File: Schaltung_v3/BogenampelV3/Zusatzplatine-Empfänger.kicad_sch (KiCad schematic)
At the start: 17 parts, among them J1 5V USB, J2 Poti 47k, J3 Poti 47k, J4 12V DCDC Boost, J5 BTN, J6 Piezo Transducter 12V, J7 LED Stripe, J8 12V FAN, Q1 BC337, U1 TSR0.5-2433, U2 XIAO ESP32C3

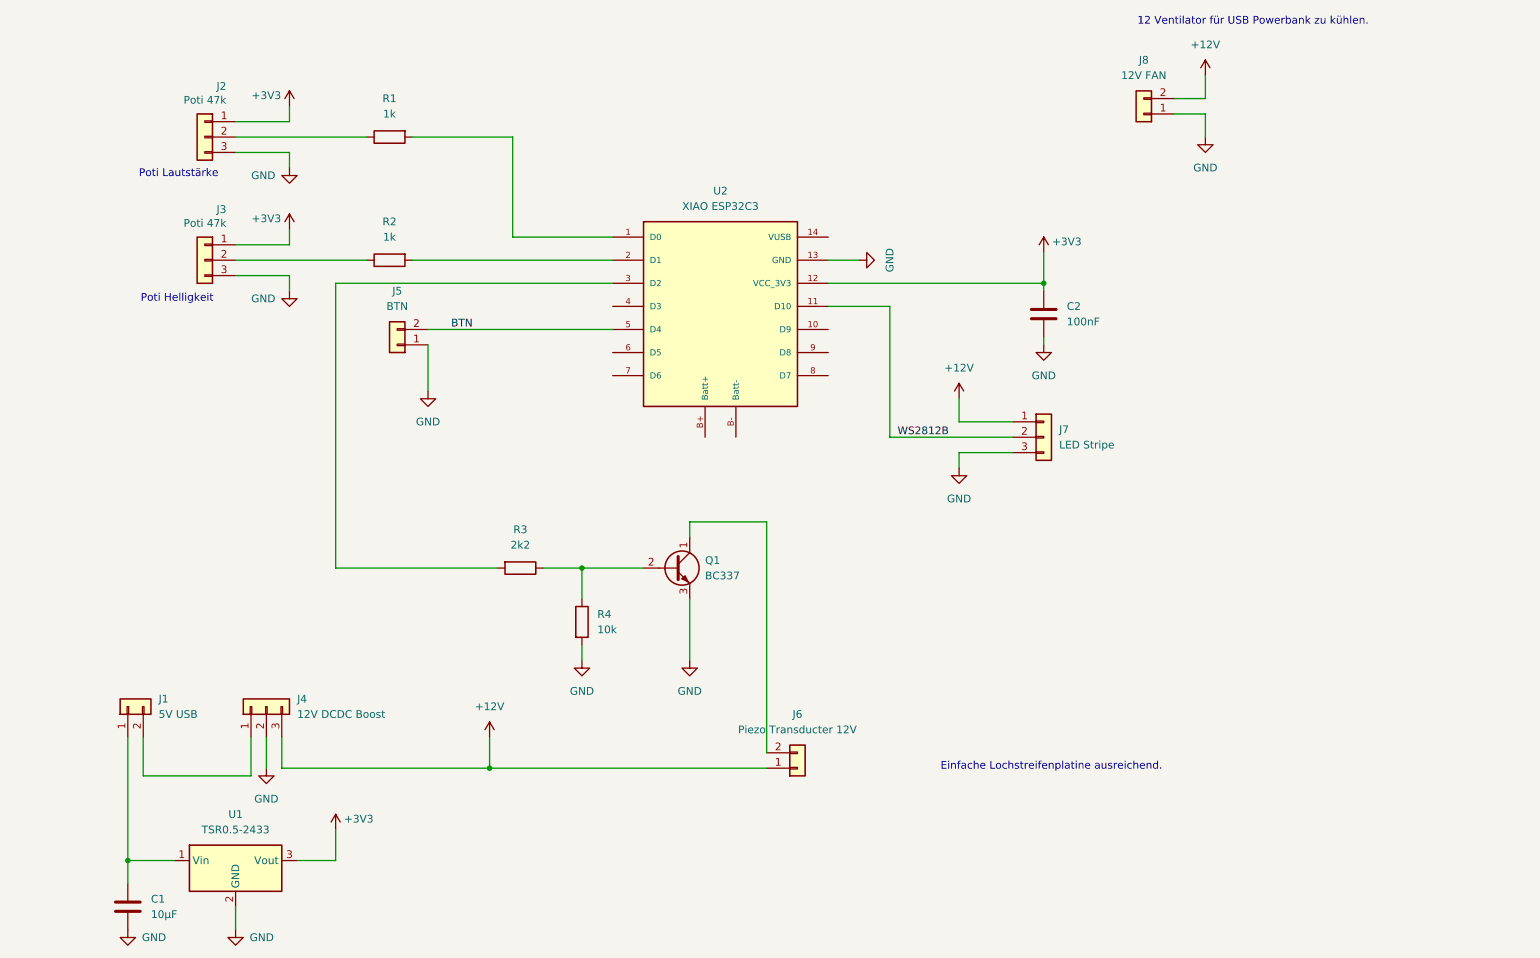
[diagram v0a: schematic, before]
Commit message: V3-Firmware: OTA, zentrales PlatformIO, .cpp-Umbenennung, Lüfter-Fix
- EmpfaengerV3 + SenderV3: .ino → .cpp (kein Konverter-Schritt mehr)
- OTA via ArduinoOTA: SoftAP-Fallback + STA-Modus (DHCP, wifi_credentials.h)
- Zentrales platformio.ini im Repo-Root (extends, build_src_filter)
- FanManager: Gate-Duty invertiert (Q2 Open-Drain, Poti-Richtung korrigiert)
- Lochrasterskizze: POTI_GND-Trennschnitt und Lüfter-Netz-Kurzschluss behoben
- KiCad: Gerber-Export, STEP-Modelle, aktualisierter Empfänger-Schaltplan
- wifi_credentials.h.example als Vorlage (echte Datei gitignored)

Co-Authored-By: Claude Sonnet 4.6 <noreply@anthropic.com>
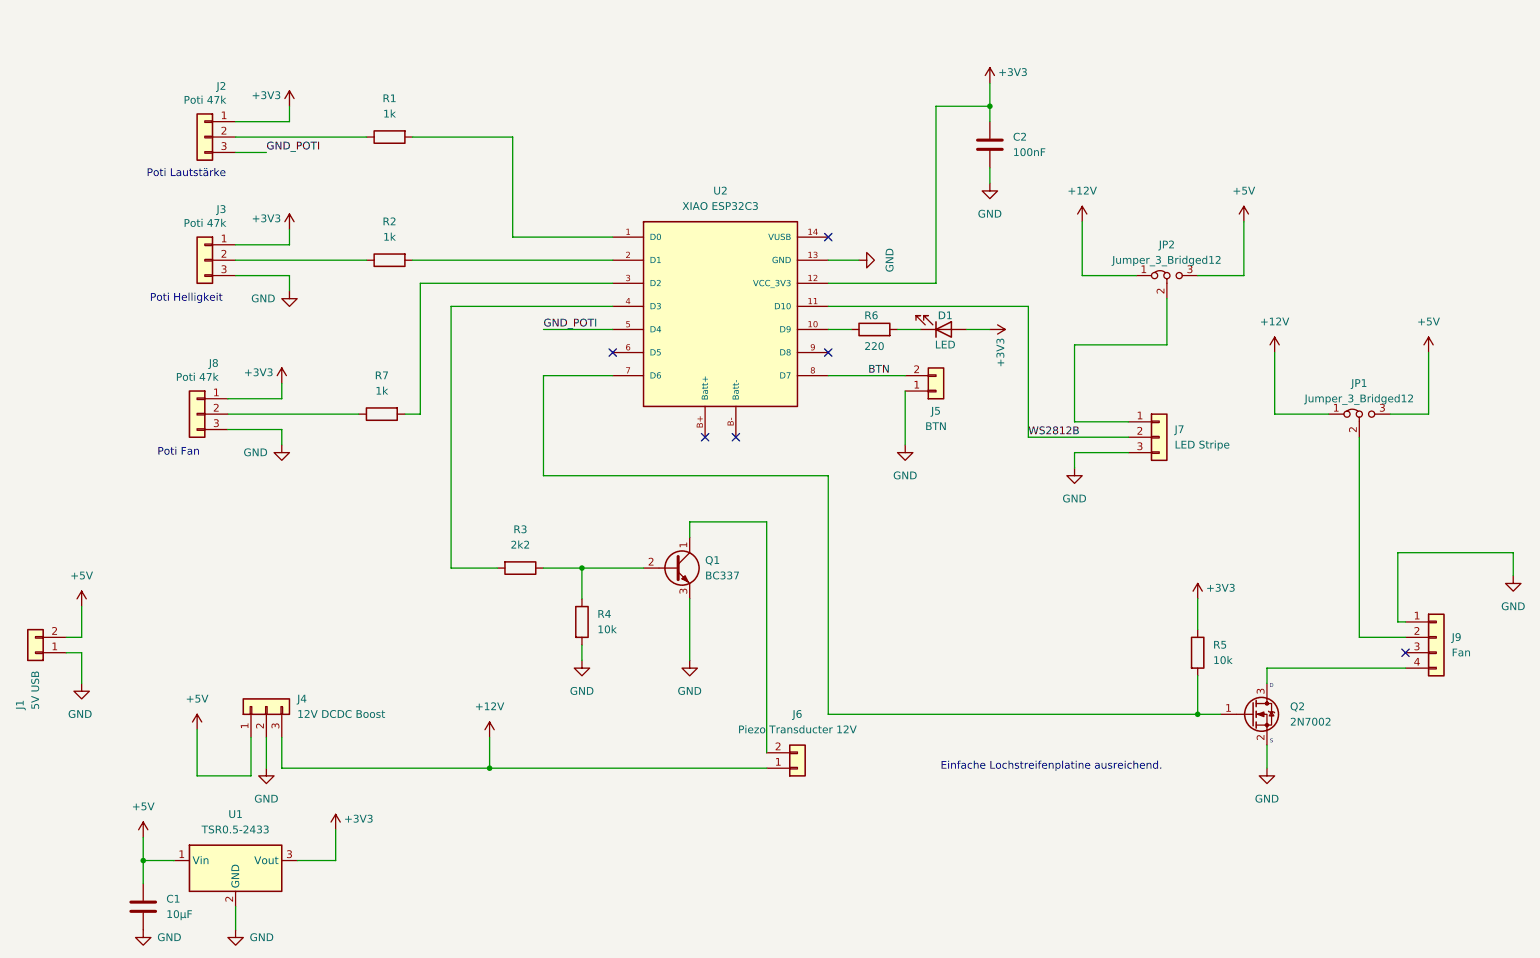
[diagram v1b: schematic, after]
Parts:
- removed J8: 12V FAN, symbol Connector_Generic:Conn_01x02
- added D1: LED, symbol Device:LED
- added J8: Poti 47k, symbol Connector_Generic:Conn_01x03
- added J9: Fan, symbol Connector_Generic:Conn_01x04
- added JP1, JP2: Jumper_3_Bridged12, symbol Jumper:Jumper_3_Bridged12
- added Q2: 2N7002, Package_TO_SOT_SMD:SOT-23, symbol PCM_MOSFET-SMD:2N7002
- added R5: 10k, symbol Device:R
- added R6: 220, symbol Device:R
- added R7: 1k, symbol Device:R
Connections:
- net +12V: now also JP1.1 (A), JP2.1 (A); no longer J7.1 (Pin_1)
- net +3V3: now also D1.2 (A), J8.1 (Pin_1), R5.1
- net BTN: now also U2.8 (D7); no longer U2.5 (D4)
- net GND: now also J1.1 (Pin_1), J8.3 (Pin_3), J9.1 (Pin_1), Q2.2 (S); no longer J2.3 (Pin_3)
- net at U2.10 (D9): now also R6.1
- net at U2.3 (D2): now also R7.2; no longer R3.2
- net at U2.4 (D3): now also R3.2
- net at U2.7 (D6): now also Q2.1 (G), R5.2
- net +5V: now reaches C1.1, U1.1 (Vin)
- net +5V: now also J1.2 (Pin_2), J4.1 (Pin_1), JP1.3 (B), JP2.3 (B); no longer J1.1 (Pin_1)
- new net: J8.2 (Pin_2), R7.1
- new net: J9.4 (Pin_4), Q2.3 (D)
- new net: D1.1 (K), R6.2
- new net: J9.2 (Pin_2), JP1.2 (C)
- new net: J7.1 (Pin_1), JP2.2 (C)
- new net GND_POTI: J2.3 (Pin_3), U2.5 (D4)
- no-connect marks 0 -> 6
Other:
- note added: "D"
- note added: "Poti Fan"
- note added: "S"
- note removed: "12 Ventilator für USB Powerbank zu kühlen."
- moved on the sheet: C1, C2, J5, J7

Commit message: Buzzer-Lautstärke: R8 (Entlade-Pfad) + Treiberfrequenz auf Resonanz 3250 Hz
Ursache des kaum hörbaren Buzzers: der Piezo (J6) am Low-Side-BC337 hatte keinen
Lade-/Entlade-Pfad. Als reine Kapazität ohne Rückweg am Collector konnte er nicht
schwingen — nur ein leises Brummen, unabhängig von Frequenz und Duty.

- HW: R8 (~1k) parallel zum Piezo / Collector→+12V ergänzt; gibt den 0↔12V-Hub
  (Zusatzplatine-Empfänger.kicad_sch, Empfaenger-Lochraster.diy, PNG-Exporte)
- FW: BUZZER_FREQUENCY_HZ 2700 -> 3250 (Resonanz CPS-4013-110PM) — am lautesten
  genau bei Resonanz (Config.h, BuzzerManager.h)

Co-Authored-By: Claude Opus 4.8 <noreply@anthropic.com>
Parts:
- added R8: 470, symbol Device:R
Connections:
- net +12V: now also R8.1
- net at J6.2 (Pin_2), Q1.1 (C): now also R8.2
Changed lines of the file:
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@@
+	)
+	(junction
+		(at 148.59 142.24)
+		(diameter 0)
+		(color 0 0 0 0)
+	)
+	(junction
+		(at 139.7 158.75)
+		(diameter 0)
+		(color 0 0 0 0)
 	)
 	(junction
@@
 	(wire
 		(pts
+			(xy 139.7 147.32) (xy 139.7 142.24)
+		)
+		(stroke
+			(width 0)
+			(type default)
+		)
+	)
+	(wire
+		(pts
 			(xy 257.81 100.33) (xy 257.81 90.17)
 		)
@@
 	(wire
 		(pts
+			(xy 139.7 142.24) (xy 148.59 142.24)
+		)
+		(stroke
+			(width 0)
+			(type default)
+		)
+	)
+	(wire
+		(pts
+			(xy 139.7 154.94) (xy 139.7 158.75)
+		)
+		(stroke
+			(width 0)
+			(type default)
+		)
+	)
+	(wire
+		(pts
 			(xy 111.76 125.73) (xy 118.11 125.73)
 		)
@@
 	(wire
 		(pts
-			(xy 102.87 158.75) (xy 148.59 158.75)
+			(xy 102.87 158.75) (xy 139.7 158.75)
 		)
 		(stroke
@@
 	(wire
 		(pts
+			(xy 139.7 158.75) (xy 148.59 158.75)
+		)
+		(stroke
+			(width 0)
+			(type default)
+		)
+	)
+	(wire
+		(pts
 			(xy 106.68 71.12) (xy 106.68 54.61)
 		)
@@
 	(wire
 		(pts
+			(xy 148.59 142.24) (xy 148.59 156.21)
+		)
+		(stroke
+			(width 0)
+			(type default)
+		)
+	)
+	(wire
+		(pts
 			(xy 111.76 93.98) (xy 123.19 93.98)
 		)
@@
 	(wire
 		(pts
-			(xy 148.59 118.11) (xy 148.59 156.21)
+			(xy 148.59 118.11) (xy 148.59 142.24)
 		)
 		(stroke
@@
 					(unit 1)
 				)
+			)
+		)
+	)
+	(symbol
+		(lib_id "Device:R")
+		(at 139.7 151.13 0)
+		(mirror x)
+		(unit 1)
+		(body_style 1)
+		(exclude_from_sim no)
+		(in_bom yes)
+		(on_board yes)
+		(in_pos_files yes)
+		(dnp no)
+		(fields_autoplaced yes)
+		(property "Reference" "R8"
+			(at 137.16 149.8599 0)
+			(show_name no)
+			(do_not_autoplace no)
+			(effects
+				(font
+					(size 1.27 1.27)
+				)
+				(justify right)
+			)
+		)
+		(property "Value" "470"
+			(at 137.16 152.3999 0)
+			(show_name no)
+			(do_not_autoplace no)
+			(effects
+				(font
+					(size 1.27 1.27)
+				)
+				(justify right)
+			)
+		)
+		(property "Footprint" ""
+			(at 137.922 151.13 90)
+			(hide yes)
+			(show_name no)
+			(do_not_autoplace no)
+			(effects
+				(font
+					(size 1.27 1.27)
+				)
+			)
+		)
+		(property "Datasheet" ""
+			(at 139.7 151.13 0)
+			(hide yes)
+			(show_name no)
+			(do_not_autoplace no)
+			(effects
+				(font
+					(size 1.27 1.27)
+				)
+			)
+		)
+		(property "Description" "Resistor"
+			(at 139.7 151.13 0)
+			(hide yes)
+			(show_name no)
+			(do_not_autoplace no)
+			(effects
+				(font
+					(size 1.27 1.27)
+				)
+			)
+		)
+		(pin "2"
+		)
+		(pin "1"
+		)
+		(instances
+			(project "Zusatzplatine-Empfänger"
+				(path "/2f5e2bd3-24fa-4ddb-a911-7a84d4c0ceae"
+					(reference "R8")
+					(unit 1)
+				)

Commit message: HW: Pull-up auf der Lüfter-PWM-Leitung ergänzt
4-Draht-Lüfter-PWM (Open-Drain über MOSFET an D6) braucht einen Pull-up auf
Logikebene (~10k nach +3,3/5 V, NICHT 12 V), damit die Steuerleitung nach HIGH
kommt — ohne den blieb sie auf 0 V und die Drehzahl ließ sich nicht regeln.
(Zusatzplatine-Empfänger.kicad_sch, Empfaenger-Lochraster.diy)

Co-Authored-By: Claude Opus 4.8 <noreply@anthropic.com>
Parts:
- added R9: 10k, symbol Device:R
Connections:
- net +3V3: now also R9.1
- net at J9.4 (Pin_4), Q2.3 (D): now also R9.2
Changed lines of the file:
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@@
 		(color 0 0 0 0)
 	)
+	(junction
+		(at 236.22 142.24)
+		(diameter 0)
+		(color 0 0 0 0)
+	)
 	(no_connect
 		(at 158.75 71.12)
@@
 	(wire
 		(pts
+			(xy 236.22 142.24) (xy 254 142.24)
+		)
+		(stroke
+			(width 0)
+			(type default)
+		)
+	)
+	(wire
+		(pts
 			(xy 139.7 154.94) (xy 139.7 158.75)
 		)
@@
 	(wire
 		(pts
+			(xy 236.22 138.43) (xy 236.22 142.24)
+		)
+		(stroke
+			(width 0)
+			(type default)
+		)
+	)
+	(wire
+		(pts
 			(xy 111.76 125.73) (xy 118.11 125.73)
 		)
@@
 	(wire
 		(pts
+			(xy 236.22 128.27) (xy 236.22 130.81)
+		)
+		(stroke
+			(width 0)
+			(type default)
+		)
+	)
+	(wire
+		(pts
 			(xy 219.71 143.51) (xy 219.71 149.86)
 		)
@@
 	(wire
 		(pts
-			(xy 231.14 142.24) (xy 254 142.24)
+			(xy 231.14 142.24) (xy 236.22 142.24)
 		)
 		(stroke
@@
 	(symbol
 		(lib_id "power:+3V3")
+		(at 236.22 128.27 0)
+		(unit 1)
+		(body_style 1)
+		(exclude_from_sim no)
+		(in_bom yes)
+		(on_board yes)
+		(in_pos_files yes)
+		(dnp no)
+		(property "Reference" "#PWR030"
+			(at 236.22 132.08 0)
+			(hide yes)
+			(show_name no)
+			(do_not_autoplace no)
+			(effects
+				(font
+					(size 1.27 1.27)
+				)
+			)
+		)
+		(property "Value" "+3V3"
+			(at 240.03 126.492 0)
+			(show_name no)
+			(do_not_autoplace no)
+			(effects
+				(font
+					(size 1.27 1.27)
+				)
+			)
+		)
+		(property "Footprint" ""
+			(at 236.22 128.27 0)
+			(hide yes)
+			(show_name no)
+			(do_not_autoplace no)
+			(effects
+				(font
+					(size 1.27 1.27)
+				)
+			)
+		)
+		(property "Datasheet" ""
+			(at 236.22 128.27 0)
+			(hide yes)
+			(show_name no)
+			(do_not_autoplace no)
+			(effects
+				(font
+					(size 1.27 1.27)
+				)
+			)
+		)
+		(property "Description" "Power symbol creates a global label with name \"+3V3\""
+			(at 236.22 128.27 0)
+			(hide yes)
+			(show_name no)
+			(do_not_autoplace no)
+			(effects
+				(font
+					(size 1.27 1.27)
+				)
+			)
+		)
+		(pin "1"
+		)
+		(instances
+			(project "Zusatzplatine-Empfänger"
+				(path "/2f5e2bd3-24fa-4ddb-a911-7a84d4c0ceae"
+					(reference "#PWR030")
+					(unit 1)
+				)
+			)
+		)
+	)
+	(symbol
+		(lib_id "power:+3V3")
 		(at 77.47 168.91 0)
 		(unit 1)
@@
 					(unit 1)
 				)
+			)
+		)
+	)
+	(symbol
+		(lib_id "Device:R")
+		(at 236.22 134.62 0)
+		(unit 1)
+		(body_style 1)
+		(exclude_from_sim no)
+		(in_bom yes)
+		(on_board yes)
+		(in_pos_files yes)
+		(dnp no)
+		(fields_autoplaced yes)
+		(property "Reference" "R9"
+			(at 238.76 133.3499 0)
+			(show_name no)
+			(do_not_autoplace no)
+			(effects
+				(font
+					(size 1.27 1.27)
+				)
+				(justify left)
+			)
+		)
+		(property "Value" "10k"
+			(at 238.76 135.8899 0)
+			(show_name no)
+			(do_not_autoplace no)
+			(effects
+				(font
+					(size 1.27 1.27)
+				)
+				(justify left)
+			)
+		)
+		(property "Footprint" ""
+			(at 234.442 134.62 90)
+			(hide yes)
+			(show_name no)
+			(do_not_autoplace no)
+			(effects
+				(font
+					(size 1.27 1.27)
+				)
+			)
+		)
+		(property "Datasheet" ""
+			(at 236.22 134.62 0)
+			(hide yes)
+			(show_name no)
+			(do_not_autoplace no)
+			(effects
+				(font
+					(size 1.27 1.27)
+				)
+			)
+		)
+		(property "Description" "Resistor"
+			(at 236.22 134.62 0)
+			(hide yes)
+			(show_name no)
+			(do_not_autoplace no)
+			(effects
+				(font
+					(size 1.27 1.27)
+				)
+			)
+		)
+		(pin "2"
+		)
+		(pin "1"
+		)
+		(instances
+			(project "Zusatzplatine-Empfänger"
+				(path "/2f5e2bd3-24fa-4ddb-a911-7a84d4c0ceae"
+					(reference "R9")
+					(unit 1)
+				)
